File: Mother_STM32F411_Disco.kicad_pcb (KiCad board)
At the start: 2 copper layers, 200 x 200 mm, 34 parts, among them U1 ESP32-DEVKIT-V1

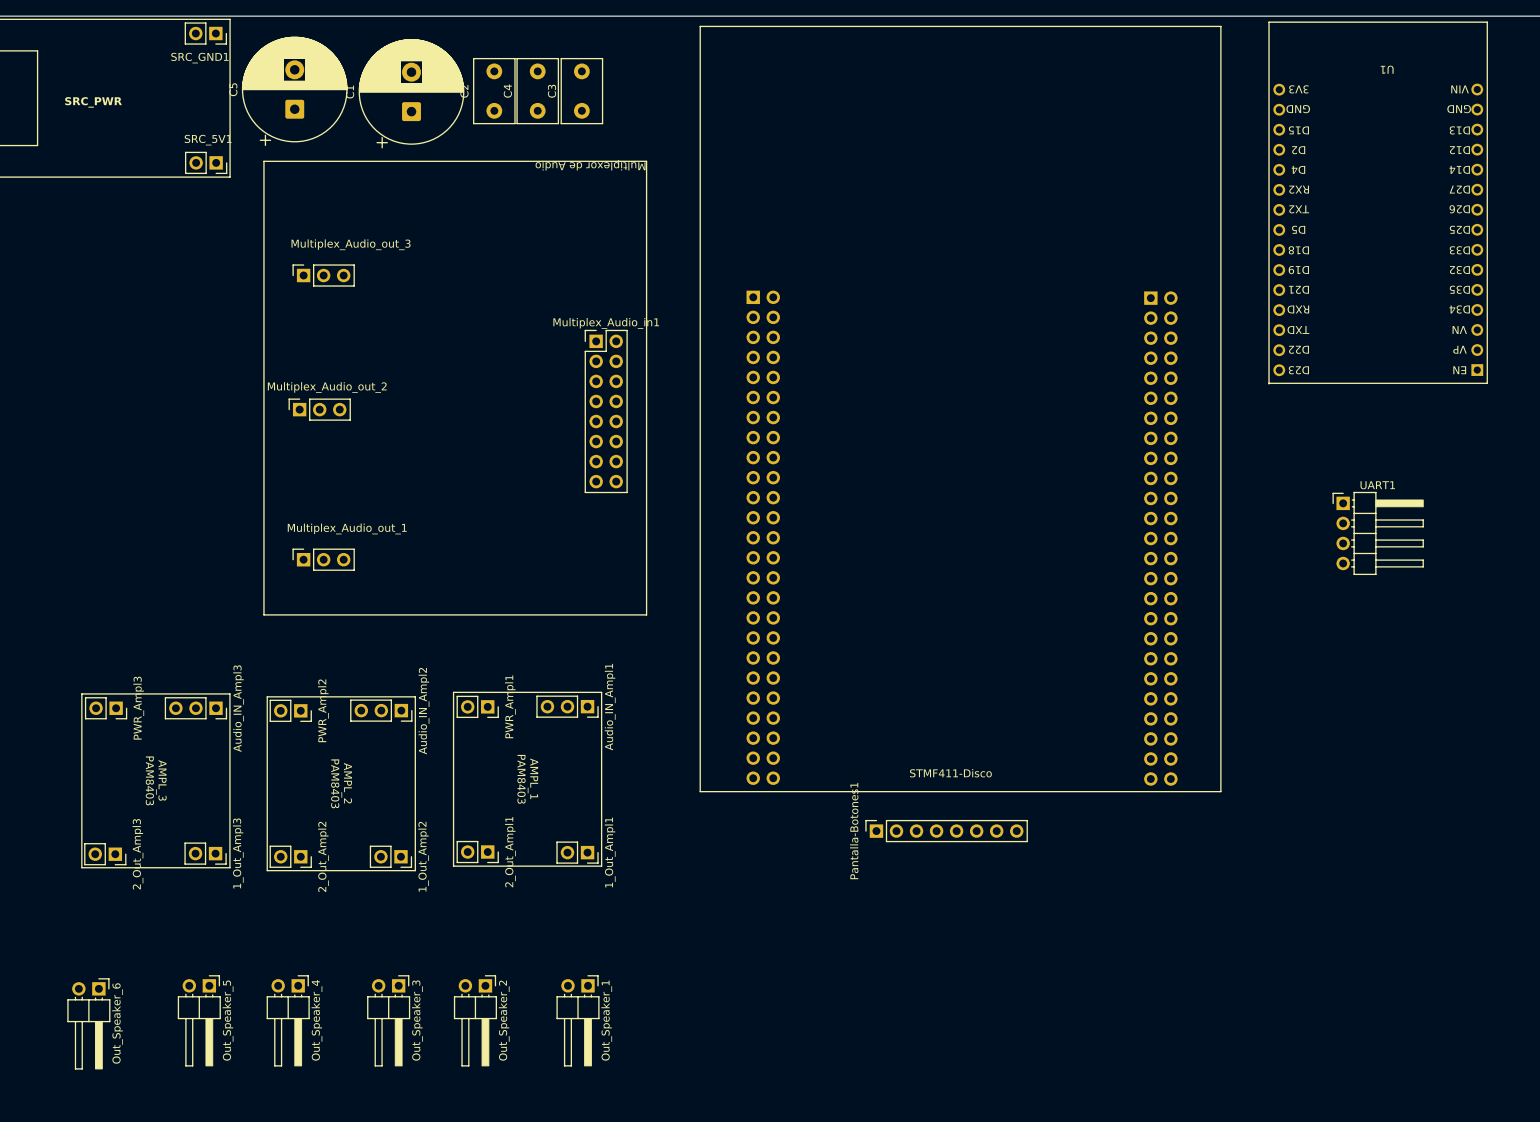
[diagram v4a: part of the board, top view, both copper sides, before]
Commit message: PCB layout preliminar
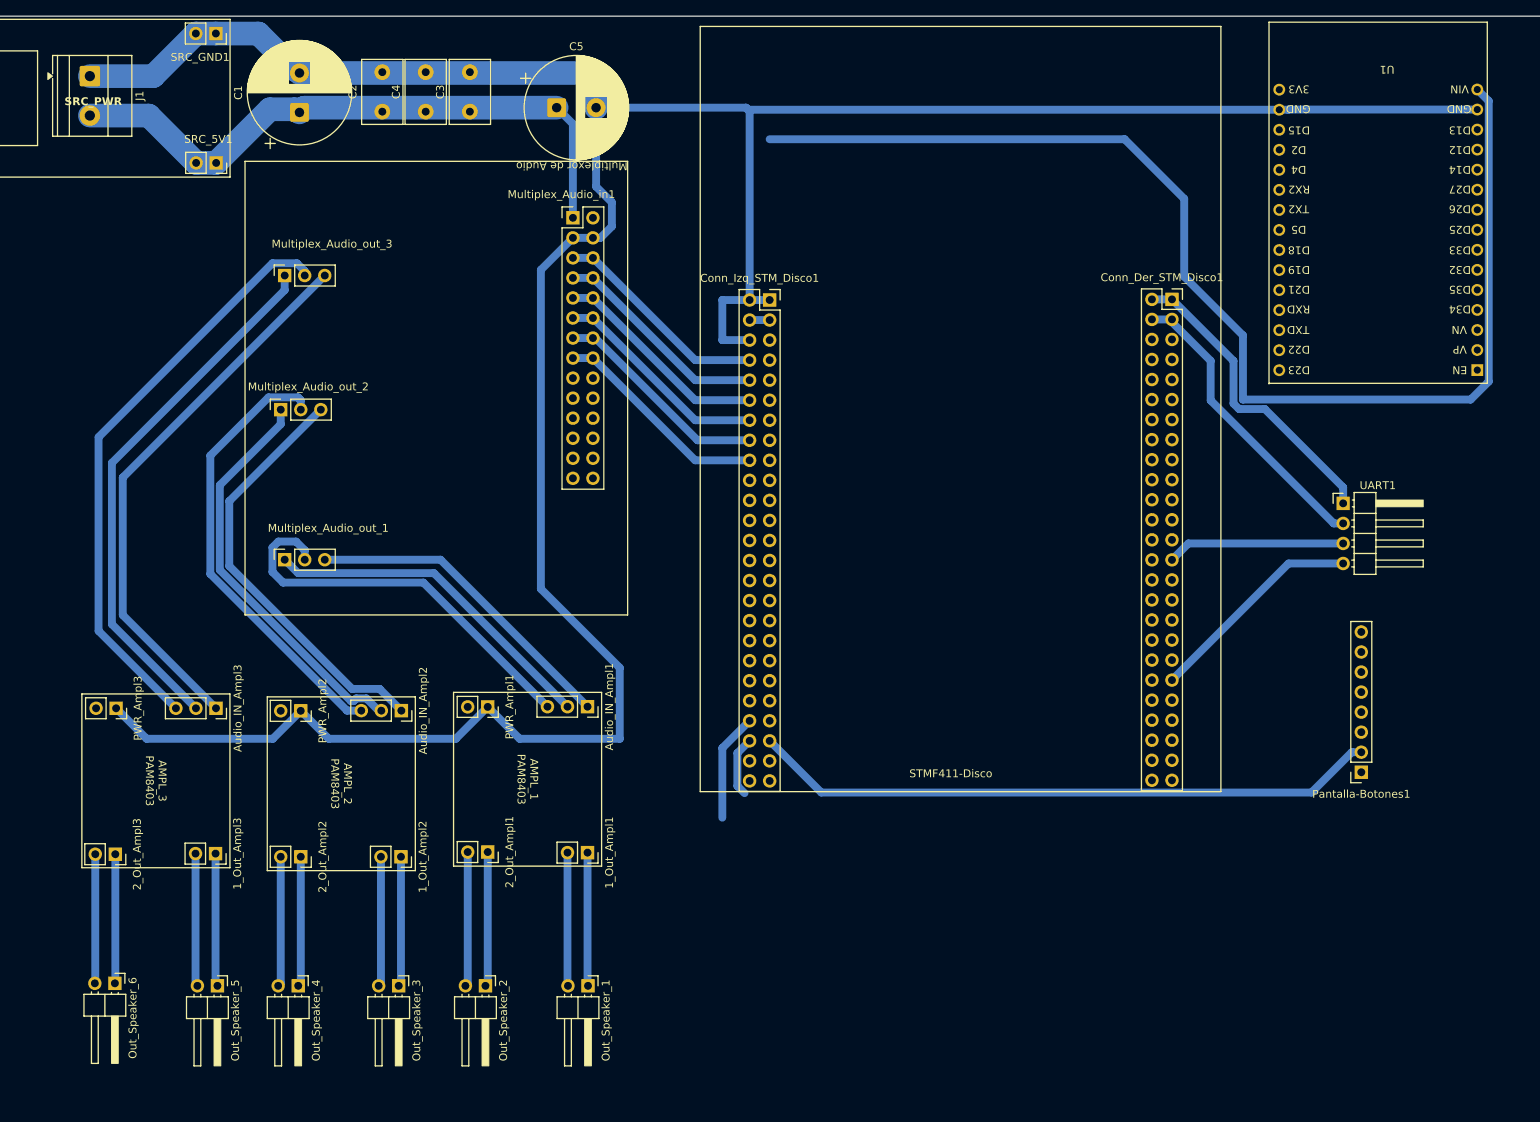
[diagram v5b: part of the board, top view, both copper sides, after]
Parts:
- added J1: SRC_Cable, TerminalBlock_Phoenix:TerminalBlock_Phoenix_MKDS-1,5-2_1x02_P5.00mm_Horizontal, F.Cu at (183.8, 35.0)
- Conn_Der_STM_Disco1, Conn_Izq_STM_Disco1: moved to F.Cu
- Multiplex_Audio_in1: value Conn_02x08_Counter_Clockwise -> Conn_02x14_Counter_Clockwise; footprint Connector_PinHeader_2.54mm:PinHeader_2x08_P2.54mm_Vertical -> Connector_PinHeader_2.54mm:PinHeader_2x14_P2.54mm_Vertical
- moved Pantalla-Botones1 61.9 mm to (345.0, 123.2), turned to 180 degrees
- moved C5 33.2 mm to (243.0, 39.0), turned to 0 degrees
- moved Multiplex_Audio_in1 15.9 mm to (245.1, 53.0)
- moved C1 14.2 mm to (210.4, 39.6)
- moved C2 14.2 mm to (220.9, 39.5)
- moved C3 14.2 mm to (232.0, 39.5)
- moved C4 14.2 mm to (226.4, 39.5)
- moved Conn_Der_STM_Disco1 2.68 mm to (321.0, 63.3), turned to 0 degrees
- moved Multiplex_Audio_out_1 2.40 mm to (208.5, 96.3)
- moved Multiplex_Audio_out_2 2.40 mm to (208.0, 77.3)
- moved Multiplex_Audio_out_3 2.40 mm to (208.5, 60.3)
- moved Out_Speaker_6 2.14 mm to (187.0, 150.0)
- moved Conn_Izq_STM_Disco1 2.11 mm to (270.0, 63.4), turned to 0 degrees
- moved Out_Speaker_5 1.03 mm to (200.0, 150.3)
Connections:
- Conn_Der_STM_Disco1 pad 10: /PC15 -> /PC14
- Conn_Der_STM_Disco1 pad 11: /PE6 -> /PC13
- Conn_Der_STM_Disco1 pad 12: /PC13 -> /PE6
- Conn_Der_STM_Disco1 pad 13: /PE4 -> /PE5
- Conn_Der_STM_Disco1 pad 14: /PE5 -> /PE4
- Conn_Der_STM_Disco1 pad 15: /PE2 -> /PE3
- Conn_Der_STM_Disco1 pad 16: /PE3 -> /PE2
- Conn_Der_STM_Disco1 pad 17: /PE0 -> /PE1
- Conn_Der_STM_Disco1 pad 18: /PE1 -> /PE0
- Conn_Der_STM_Disco1 pad 19: /PB8 -> /PB9
- Conn_Der_STM_Disco1 pad 20: /PB9 -> /PB8
- Conn_Der_STM_Disco1 pad 21: /BOOT0 -> /VDD
- Conn_Der_STM_Disco1 pad 22: /VDD -> /BOOT0
- Conn_Der_STM_Disco1 pad 23: /PB6 -> /PB7
- Conn_Der_STM_Disco1 pad 24: /PB7 -> /PB6
- Conn_Der_STM_Disco1 pad 25: /PB4 -> /PB5
- Conn_Der_STM_Disco1 pad 26: /PB5 -> /PB4
- Conn_Der_STM_Disco1 pad 27: /PD7 -> /PB3
- Conn_Der_STM_Disco1 pad 28: /PB3 -> /PD7
- Conn_Der_STM_Disco1 pad 29: /PD5 -> /PD6
- Conn_Der_STM_Disco1 pad 30: /PD6 -> /PD5
- Conn_Der_STM_Disco1 pad 31: /PD3 -> /PD4
- Conn_Der_STM_Disco1 pad 32: /PD4 -> /PD3
- Conn_Der_STM_Disco1 pad 33: /PD1 -> /PD2
- Conn_Der_STM_Disco1 pad 34: /PD2 -> /PD1
- Conn_Der_STM_Disco1 pad 35: /PC12 -> /PD0
- Conn_Der_STM_Disco1 pad 36: /PD0 -> /PC12
- Conn_Der_STM_Disco1 pad 37: /PC10 -> /PC11
- Conn_Der_STM_Disco1 pad 38: /PC11 -> /PC10
- Conn_Der_STM_Disco1 pad 39: /PA14 -> /PA15
- Conn_Der_STM_Disco1 pad 40: /PA15 -> /PA14
- Conn_Der_STM_Disco1 pad 41: /PA10 -> /PA13
- Conn_Der_STM_Disco1 pad 42: /PA13 -> /PA10
- Conn_Der_STM_Disco1 pad 43: /PA8 -> /PA9
- Conn_Der_STM_Disco1 pad 44: /PA9 -> /PA8
- Conn_Der_STM_Disco1 pad 45: /PC8 -> /PC9
- Conn_Der_STM_Disco1 pad 46: /PC9 -> /PC8
- Conn_Der_STM_Disco1 pad 47: /PC6 -> /PC7
- Conn_Der_STM_Disco1 pad 48: /PC7 -> /PC6
- Conn_Der_STM_Disco1 pad 7: /PH0 -> /PH1
- Conn_Der_STM_Disco1 pad 8: /PH1 -> /PH0
- Conn_Der_STM_Disco1 pad 9: /PC14 -> /PC15
- Conn_Izq_STM_Disco1 pad 10: /PC2 -> /PC3
- Conn_Izq_STM_Disco1 pad 11: /PA1 -> /PA0
- Conn_Izq_STM_Disco1 pad 12: /PA0 -> /PA1
- Conn_Izq_STM_Disco1 pad 13: /PA3 -> /PA2
- Conn_Izq_STM_Disco1 pad 14: /PA2 -> /PA3
- Conn_Izq_STM_Disco1 pad 15: /PA5 -> /PA4
- Conn_Izq_STM_Disco1 pad 16: /PA4 -> /PA5
- Conn_Izq_STM_Disco1 pad 17: /PA7 -> /PA6
- Conn_Izq_STM_Disco1 pad 18: /PA6 -> /PA7
- Conn_Izq_STM_Disco1 pad 19: /PC5 -> /PC4
- Conn_Izq_STM_Disco1 pad 20: /PC4 -> /PC5
- Conn_Izq_STM_Disco1 pad 21: /PB1 -> /PB0
- Conn_Izq_STM_Disco1 pad 22: /PB0 -> /PB1
- Conn_Izq_STM_Disco1 pad 23: /GND -> /PB2
- Conn_Izq_STM_Disco1 pad 24: /PB2 -> /GND
- Conn_Izq_STM_Disco1 pad 25: /PE7 -> /PE8
- Conn_Izq_STM_Disco1 pad 26: /PE8 -> /PE7
- Conn_Izq_STM_Disco1 pad 27: /PE9 -> /PE10
- Conn_Izq_STM_Disco1 pad 28: /PE10 -> /PE9
- Conn_Izq_STM_Disco1 pad 29: /PE11 -> /PE12
- Conn_Izq_STM_Disco1 pad 30: /PE12 -> /PE11
- Conn_Izq_STM_Disco1 pad 31: /PE13 -> /PE14
- Conn_Izq_STM_Disco1 pad 32: /PE14 -> /PE13
- Conn_Izq_STM_Disco1 pad 33: /PE15 -> /PB10
- Conn_Izq_STM_Disco1 pad 34: /PB10 -> /PE15
- Conn_Izq_STM_Disco1 pad 35: /NC -> /PB12
- Conn_Izq_STM_Disco1 pad 36: /PB12 -> /NC
- Conn_Izq_STM_Disco1 pad 37: /PB13 -> /PB14
- Conn_Izq_STM_Disco1 pad 38: /PB14 -> /PB13
- Conn_Izq_STM_Disco1 pad 39: /PB15 -> /PD8
- Conn_Izq_STM_Disco1 pad 40: /PD8 -> /PB15
- Conn_Izq_STM_Disco1 pad 41: /PD9 -> /PD10
- Conn_Izq_STM_Disco1 pad 42: /PD10 -> /PD9
- Conn_Izq_STM_Disco1 pad 43: /PD11 -> /PD12
- Conn_Izq_STM_Disco1 pad 44: /PD12 -> /PD11
- Conn_Izq_STM_Disco1 pad 45: /PD13 -> /PD14
- Conn_Izq_STM_Disco1 pad 46: /PD14 -> /PD13
- Conn_Izq_STM_Disco1 pad 47: /PD15 -> /NC
- Conn_Izq_STM_Disco1 pad 48: /NC -> /PD15
- Conn_Izq_STM_Disco1 pad 5: /GND -> /NRST
- Conn_Izq_STM_Disco1 pad 6: /NRST -> /GND
- Conn_Izq_STM_Disco1 pad 7: /PC1 -> /PC0
- Conn_Izq_STM_Disco1 pad 8: /PC0 -> /PC1
- Conn_Izq_STM_Disco1 pad 9: /PC3 -> /PC2
- Multiplex_Audio_in1 pad 10: unconnected-(Multiplex_Audio_in1-Pin_10-Pad10) -> /PA1
- Multiplex_Audio_in1 pad 12: unconnected-(Multiplex_Audio_in1-Pin_12-Pad12) -> /PA3
- Multiplex_Audio_in1 pad 14: unconnected-(Multiplex_Audio_in1-Pin_14-Pad14) -> /PA5
- Multiplex_Audio_in1 pad 16: unconnected-(Multiplex_Audio_in1-Pin_16-Pad16) -> /PA7
- Multiplex_Audio_in1 pad 4: unconnected-(Multiplex_Audio_in1-Pin_4-Pad4) -> /GND
- Multiplex_Audio_in1 pad 6: unconnected-(Multiplex_Audio_in1-Pin_6-Pad6) -> /PC1
- Multiplex_Audio_in1 pad 8: unconnected-(Multiplex_Audio_in1-Pin_8-Pad8) -> /PC3
- Out_Speaker_1 pad 1: Net-(1_Out_Ampl1-Pin_2) -> Net-(1_Out_Ampl1-Pin_1)
- Out_Speaker_1 pad 2: Net-(1_Out_Ampl1-Pin_1) -> Net-(1_Out_Ampl1-Pin_2)
- Out_Speaker_2 pad 1: Net-(2_Out_Ampl1-Pin_2) -> Net-(2_Out_Ampl1-Pin_1)
- Out_Speaker_2 pad 2: Net-(2_Out_Ampl1-Pin_1) -> Net-(2_Out_Ampl1-Pin_2)
- Out_Speaker_3 pad 1: Net-(1_Out_Ampl2-Pin_2) -> Net-(1_Out_Ampl2-Pin_1)
- Out_Speaker_3 pad 2: Net-(1_Out_Ampl2-Pin_1) -> Net-(1_Out_Ampl2-Pin_2)
- Out_Speaker_4 pad 1: Net-(2_Out_Ampl2-Pin_2) -> Net-(2_Out_Ampl2-Pin_1)
- Out_Speaker_4 pad 2: Net-(2_Out_Ampl2-Pin_1) -> Net-(2_Out_Ampl2-Pin_2)
- Out_Speaker_5 pad 1: Net-(1_Out_Ampl3-Pin_2) -> Net-(1_Out_Ampl3-Pin_1)
- Out_Speaker_5 pad 2: Net-(1_Out_Ampl3-Pin_1) -> Net-(1_Out_Ampl3-Pin_2)
- Out_Speaker_6 pad 1: Net-(2_Out_Ampl3-Pin_2) -> Net-(2_Out_Ampl3-Pin_1)
- Out_Speaker_6 pad 2: Net-(2_Out_Ampl3-Pin_1) -> Net-(2_Out_Ampl3-Pin_2)
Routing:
- net /GND: track 0.00 -> 424.6 mm
- net /5V: track 0.00 -> 271.0 mm
- net /PD14: track 0.00 -> 79.8 mm
- net Net-(Audio_IN_Ampl3-Pin_3): track 0.00 -> 74.7 mm
- net Net-(Audio_IN_Ampl3-Pin_1): track 0.00 -> 70.4 mm
- net Net-(Audio_IN_Ampl3-Pin_2): track 0.00 -> 68.3 mm
- net Net-(Audio_IN_Ampl2-Pin_3): track 0.00 -> 57.2 mm
- net Net-(Audio_IN_Ampl2-Pin_1): track 0.00 -> 54.0 mm
- net Net-(Audio_IN_Ampl2-Pin_2): track 0.00 -> 51.7 mm
- net Net-(Audio_IN_Ampl1-Pin_3): track 0.00 -> 51.1 mm
- net Net-(Audio_IN_Ampl1-Pin_2): track 0.00 -> 43.6 mm
- net Net-(Audio_IN_Ampl1-Pin_1): track 0.00 -> 41.0 mm
- net /PA15: track 0.00 -> 27.8 mm
- net /PC3: track 0.00 -> 27.8 mm
- net /PA7: track 0.00 -> 27.8 mm
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
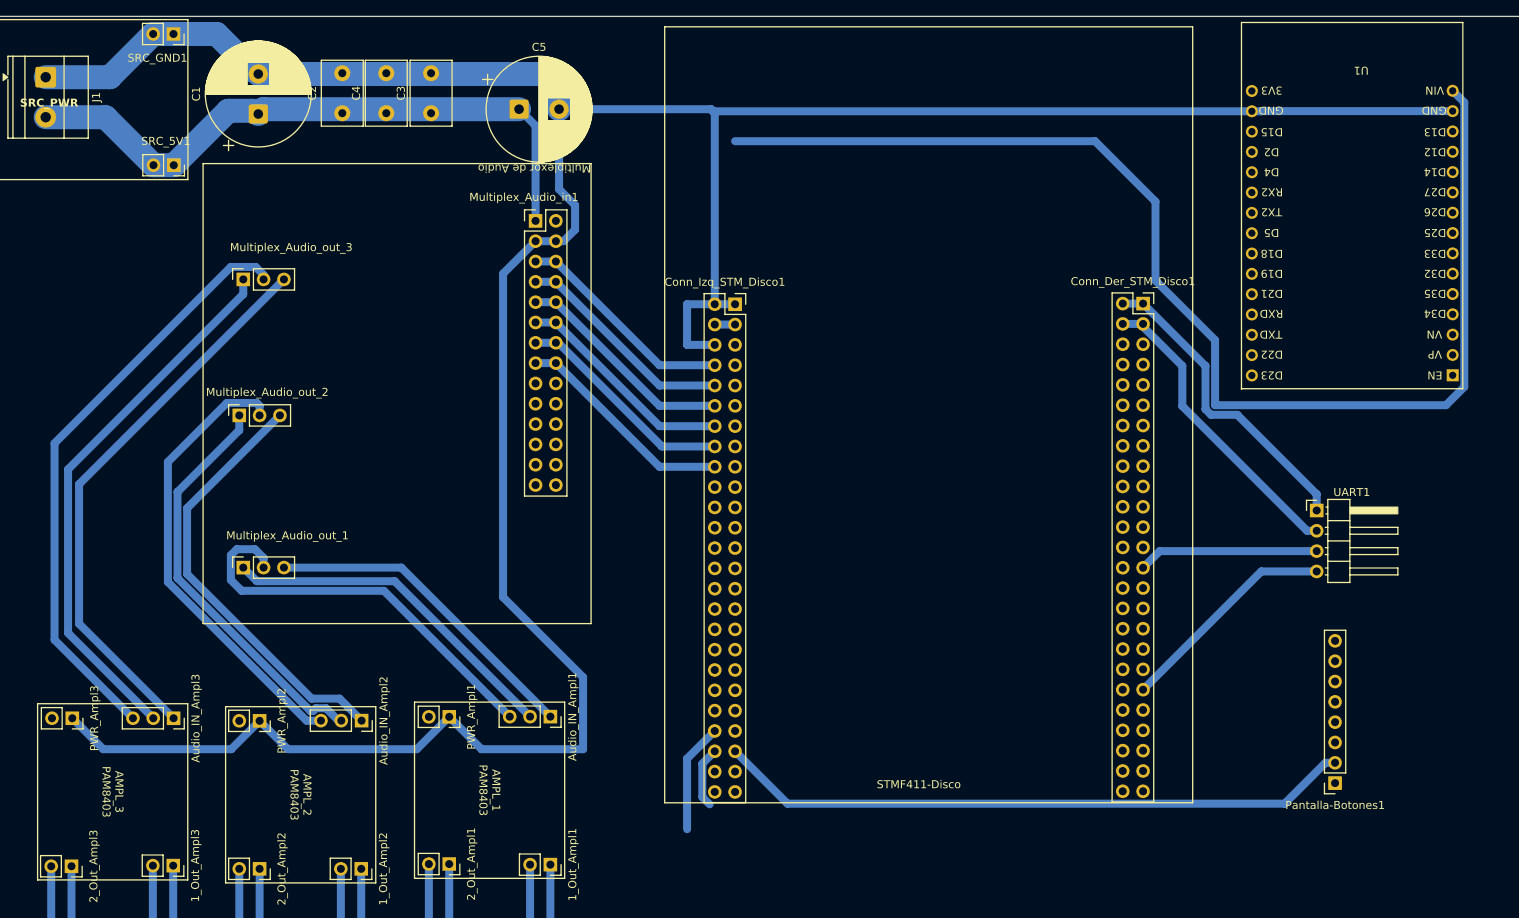
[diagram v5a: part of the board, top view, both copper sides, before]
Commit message: Huellas OK, PCB layout OK
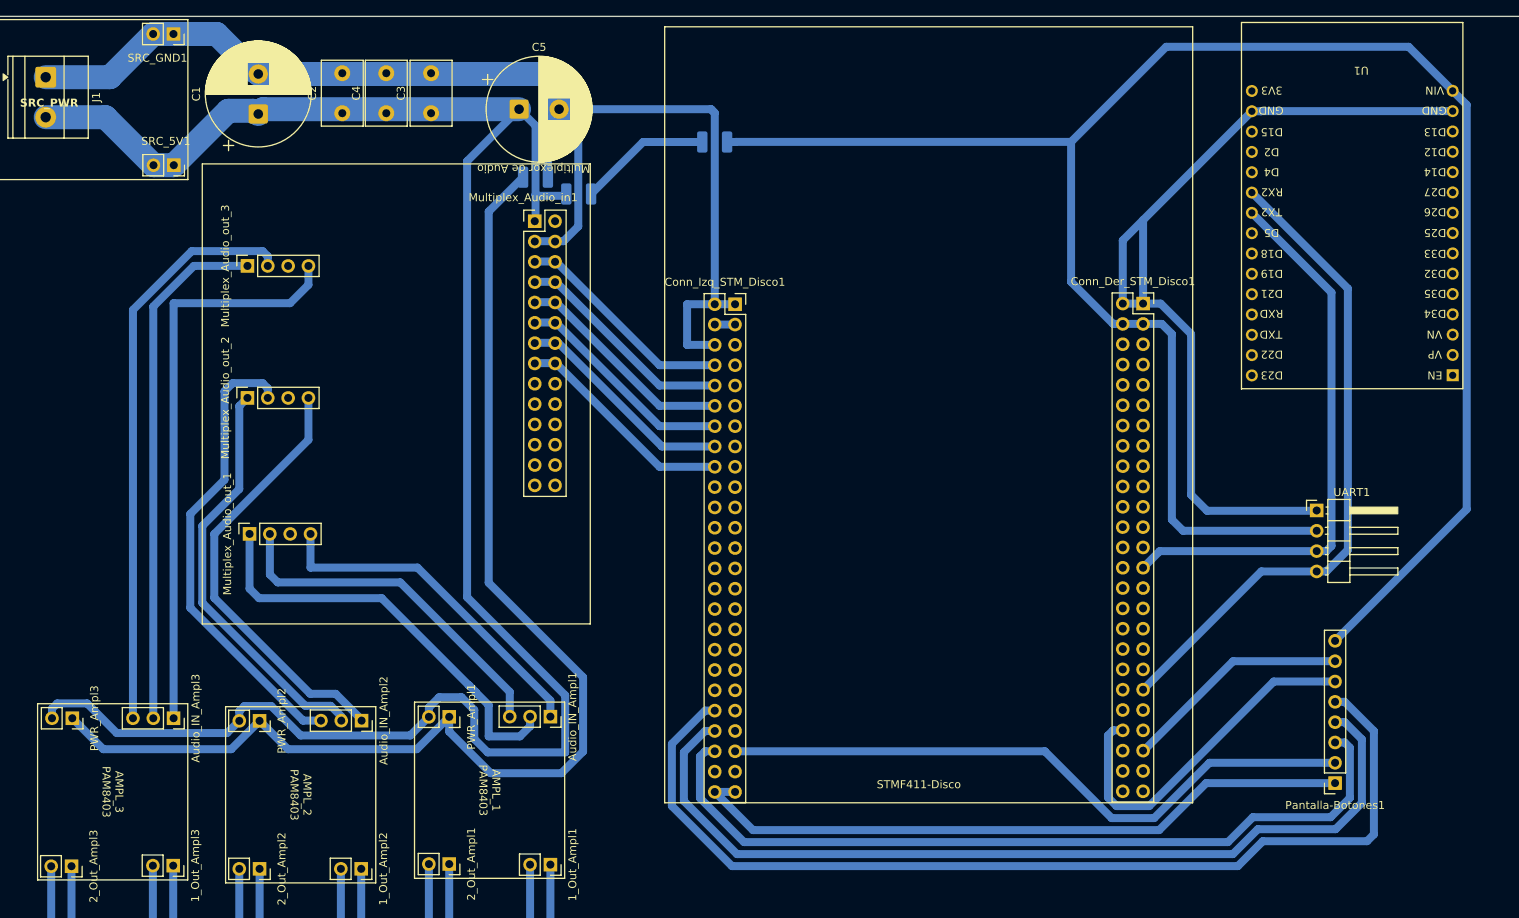
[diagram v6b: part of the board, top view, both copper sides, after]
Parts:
- added J2: 0, Resistor_SMD:R_1210_3225Metric_Pad1.30x2.65mm_HandSolder, B.Cu at (267.4, 43.1)
- added J3: 0, Resistor_SMD:R_1210_3225Metric_Pad1.30x2.65mm_HandSolder, B.Cu at (245.1, 47.5)
- added J4: 0, Resistor_SMD:R_1210_3225Metric_Pad1.30x2.65mm_HandSolder, B.Cu at (250.4, 49.6)
- Multiplex_Audio_out_1, Multiplex_Audio_out_2, Multiplex_Audio_out_3: value Conn_01x03 -> Conn_01x04; footprint Connector_PinSocket_2.54mm:PinSocket_1x03_P2.54mm_Vertical -> Connector_PinSocket_2.54mm:PinSocket_1x04_P2.54mm_Vertical
- moved Multiplex_Audio_out_1 4.28 mm to (209.3, 92.1)
- moved Multiplex_Audio_out_2 2.41 mm to (209.1, 75.1)
- moved Multiplex_Audio_out_3 1.76 mm to (209.1, 58.6)
- moved Multiplex_Audio_in1 0.11 mm to (245.0, 53.0)
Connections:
- Conn_Der_STM_Disco1 pad 21: /VDD -> /VDD_2
- Multiplex_Audio_out_1 pad 3: Net-(Audio_IN_Ampl1-Pin_1) -> unconnected-(Multiplex_Audio_out_1-Pin_3-Pad3)
- Multiplex_Audio_out_2 pad 3: Net-(Audio_IN_Ampl2-Pin_1) -> unconnected-(Multiplex_Audio_out_2-Pin_3-Pad3)
- Multiplex_Audio_out_3 pad 3: Net-(Audio_IN_Ampl3-Pin_1) -> unconnected-(Multiplex_Audio_out_3-Pin_3-Pad3)
- PWR_Ampl1 pad 1: /GND -> /GND_Analg
- PWR_Ampl2 pad 1: /GND -> /GND_Analg
- PWR_Ampl3 pad 1: /GND -> /GND_Analg
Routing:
- net /5V: track 271.0 -> 515.3 mm
- net /GND_Analg: track 0.00 -> 153.6 mm
- net /PD9: track 0.00 -> 126.6 mm
- net /PD11: track 13.7 -> 113.4 mm
- net /PD13: track 7.65 -> 101.5 mm
- net /GND: track 424.6 -> 358.7 mm
- net /PA15: track 27.8 -> 82.5 mm
- net /PB3: track 22.6 -> 70.4 mm
- net /PA8: track 0.00 -> 45.1 mm
- net /PC9: track 0.00 -> 28.6 mm
- net Net-(Audio_IN_Ampl1-Pin_2): track 43.6 -> 53.6 mm
- net Net-(Audio_IN_Ampl1-Pin_3): track 51.1 -> 44.2 mm
- net Net-(Audio_IN_Ampl3-Pin_2): track 68.3 -> 65.3 mm
- net Net-(Audio_IN_Ampl3-Pin_3): track 74.7 -> 72.4 mm
- net Net-(Audio_IN_Ampl1-Pin_1): track 41.0 -> 43.1 mm
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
